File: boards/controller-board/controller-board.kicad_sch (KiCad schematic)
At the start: 170 parts, among them J1 Conn_01x02, J2 Conn_01x02, J3 Conn_01x02, J4 Conn_01x02, J5 Conn_01x03, J6 Conn_01x02, Q1 Goford_G11S_20V_11A, Q2 PMV45EN, SW1 EG1271, U1 CAT4201, U10 CAT4201, U11 CAT4201, U12 CAT4201, U13 CAT4201, U14 CAT4201, U15 CAT4201, U17 CAT4201, U18 CAT4201, U25 RPi_Pico, U3 LTC3624, U4 CAT4201, U5 CAT4201, U6 CAT4201, U7 MCP4728, U8 ADS1015IRUGR, U9 ADS1015IRUGR

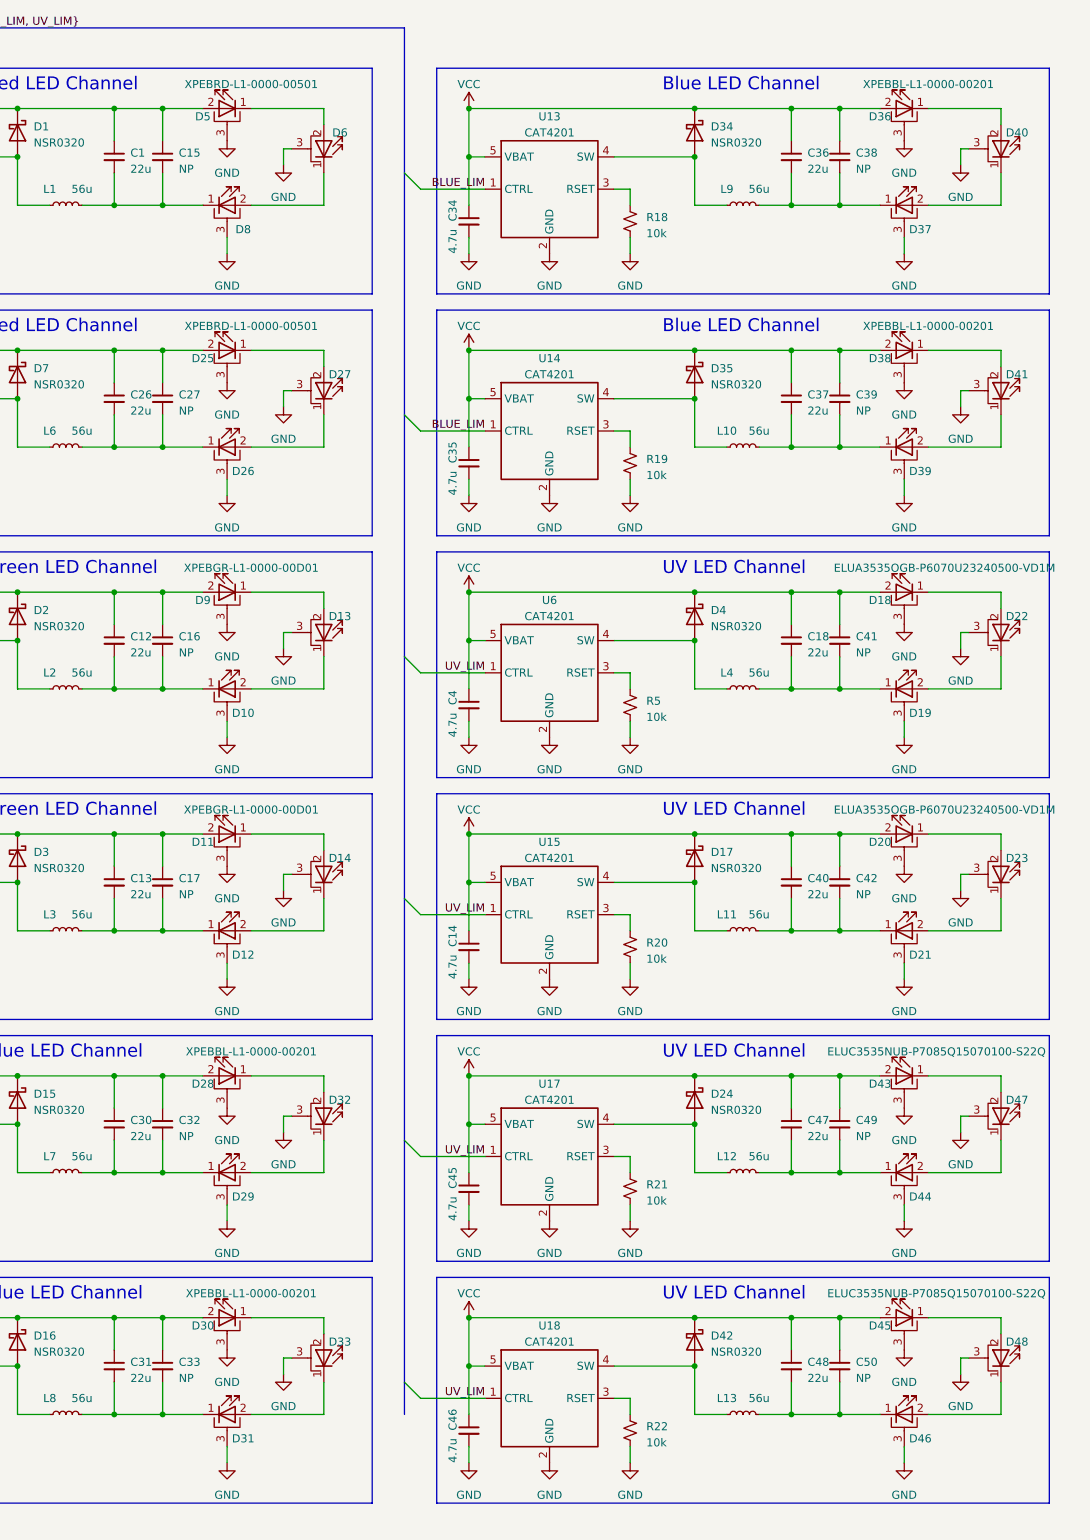
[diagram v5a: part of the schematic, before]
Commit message: moved LED driver circuitry to front layer of PCB
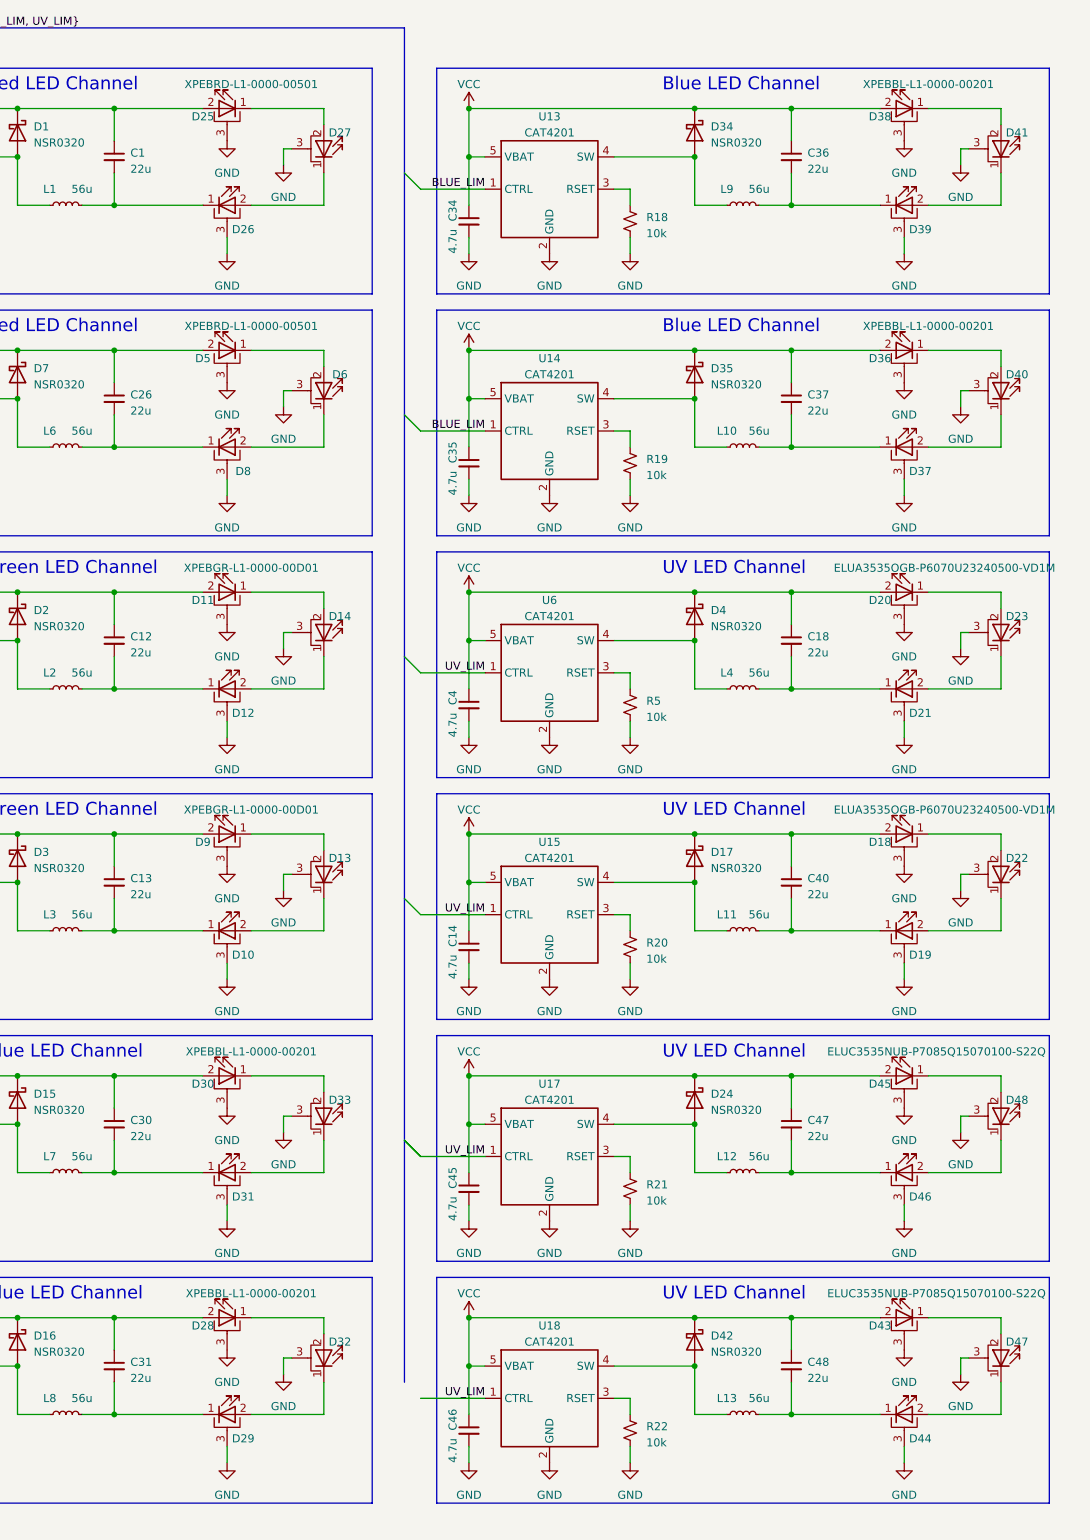
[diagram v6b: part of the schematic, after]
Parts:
- removed C15, C16, C17, C27, C32, C33, C38, C39, C41, C42, C49, C50: NP, Capacitor_THT:C_Radial_D10.0mm_H16.0mm_P5.00mm, symbol Device:C_Small
- C51: footprint (none) -> Capacitor_SMD:C_0603_1608Metric
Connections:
- net GND: now also Q1.2, Q1.3
- net at C12.2, L2.2: now also D12.1 (K); no longer D10.1 (K)
- net at C30.2, L7.2: now also D31.1 (K); no longer D29.1 (K)
- net at C48.2, L13.2: now also D44.1 (K); no longer D46.1 (K)
- net at C18.2, L4.2: now also D21.1 (K); no longer D19.1 (K)
- net at C40.2, L11.2: now also D19.1 (K); no longer D21.1 (K)
- net at C31.2, L8.2: now also D29.1 (K); no longer D31.1 (K)
- net at J6.1 (Pin_1), Q1.5: now also Q1.6, Q1.7, Q1.8
- net at C47.2, L12.2: now also D46.1 (K); no longer D44.1 (K)
- net at C37.2, L10.2: now also D37.1 (K); no longer D39.1 (K)
- net at C36.2, L9.2: now also D39.1 (K); no longer D37.1 (K)
- net at C13.2, L3.2: now also D10.1 (K); no longer D12.1 (K)
- net at C1.2, L1.2: now also D26.1 (K); no longer D8.1 (K)
- net at C26.2, L6.2: now also D8.1 (K); no longer D26.1 (K)
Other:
- moved on the sheet: D10, D11, D12, D13, D14, D18, D19, D20, D21, D22, D23, D25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

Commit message: Fxied halogen PWM, made SPS DNP, some schematic polishing.
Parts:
- C10, C21, C22, C5, C6, C7, C8, C9, L5, R8, R9, SW1, U3, U9: now not fitted; now left out of the parts list
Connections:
- net GND: now also J6.1 (Pin_1); no longer Q1.1 (S), Q1.2, Q1.3
- net VCC: now also Q1.1 (S), Q1.2, Q1.3; no longer J6.2 (Pin_2)
- net PWM: now reaches Q2.1 (G), R11.1, U25.34 (GPIO28_ADC2)
- net at Q1.5, Q1.6, Q1.7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: now also J6.2 (Pin_2); no longer J6.1 (Pin_1)
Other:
- note added: "+12V @ 6A"
- note added: "To 75 W 12 V Halogen"
- note removed: "+12V"
- note removed: "CLK and MISO are used as GPIO pins"
- moved on the sheet: C19, C23, C24, F1, J1, J2, J3, J4, J5, J6, Q1, R1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

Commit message: added test points
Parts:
- added TP10, TP11, TP12, TP13, TP8: TestPoint-MinTH, oresat-misc:TestPoint-MinTH, symbol oresat-misc:TestPoint-MinTH
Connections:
- net at U25.1 (GPIO0): now also TP8.1
- net at U25.2 (GPIO1): now also TP10.1
- net at U25.4 (GPIO2): now also TP11.1
- net at U25.5 (GPIO3): now also TP12.1
- net at U25.6 (GPIO4): now also TP13.1
- no-connect marks 31 -> 26
